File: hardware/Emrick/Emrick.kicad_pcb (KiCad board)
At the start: 4 copper layers, 41.5 x 74.1 mm, 88 parts, among them J1 LED_STRIP_CONNECTOR, J2 UFL, J3 Conn_02x05_Odd_Even, J4 BATT_CONN, P1 USB_C_Plug_USB2.0, Q1 Q_NMOS_GSD, Q2 Q_NMOS_GSD, Q3 Q_NMOS_GSD, SW1 SW_SPST, U1 74HCT541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

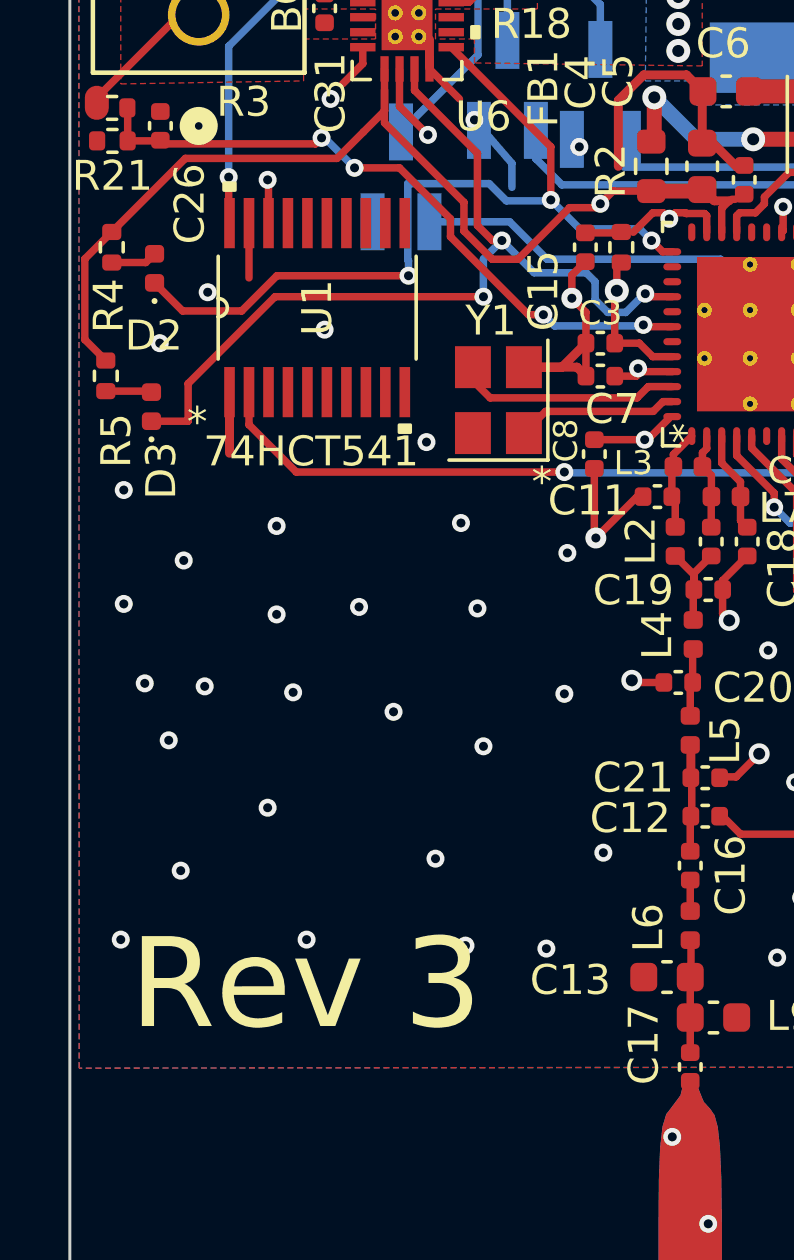
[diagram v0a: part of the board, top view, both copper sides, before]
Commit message: Fix floating GND connection
Added a via to fix a floating GND fill that wasn't connecting the GND pin of the battery voltage divider.
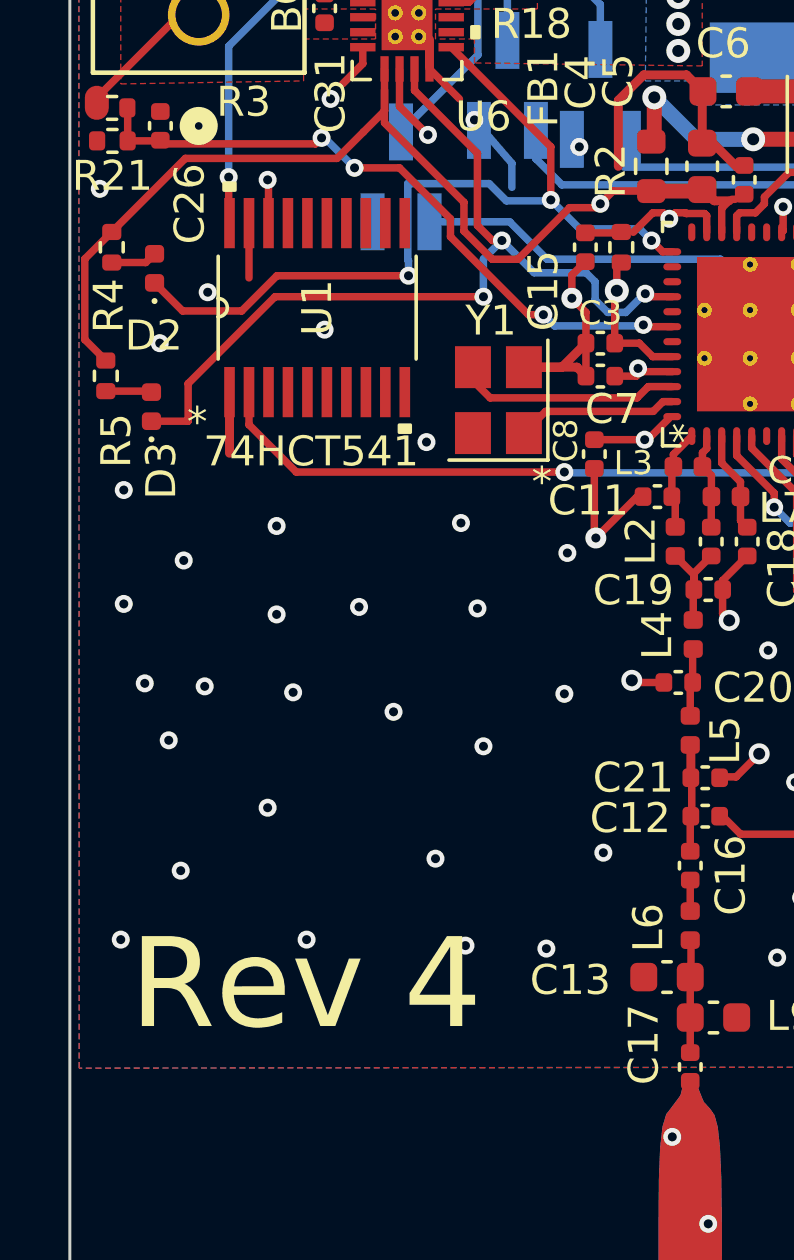
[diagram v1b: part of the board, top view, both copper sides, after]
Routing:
- net GND: vias 86 -> 87
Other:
- board text added: "Rev 4"
- board text removed: "Rev 3"
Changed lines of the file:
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@@
     (title "Emrick")
     (date "2022-10-13")
-    (rev "3")
+    (rev "4")
     (company "Erik Duxstad, Zareef Huq")
     (comment 1 "Layer Stackup: JLC04161H-7628")
@@
     (effects (font (size 1 1) (thickness 0.15)))
   )
-  (gr_text "Rev 3" (at 83.7 63.1) (layer "F.SilkS")
+  (gr_text "Rev 4" (at 83.7 63.1) (layer "F.SilkS")
     (effects (font (size 3 3) (thickness 0.3)) (justify left bottom))
   )
@@
   (via (at 109.95 34.7) (size 0.6) (drill 0.3) (layers "F.Cu" "B.Cu") (net 2))
   (via (at 91.35 48.75) (size 0.6) (drill 0.3) (layers "F.Cu" "B.Cu") (free) (net 2))
+  (via (at 82.7 34.8) (size 0.6) (drill 0.3) (layers "F.Cu" "B.Cu") (free) (net 2))
   (via (at 112.3 58.45) (size 0.6) (drill 0.3) (layers "F.Cu" "B.Cu") (free) (net 2))
   (via (at 111 44.05) (size 0.6) (drill 0.3) (layers "F.Cu" "B.Cu") (net 2))

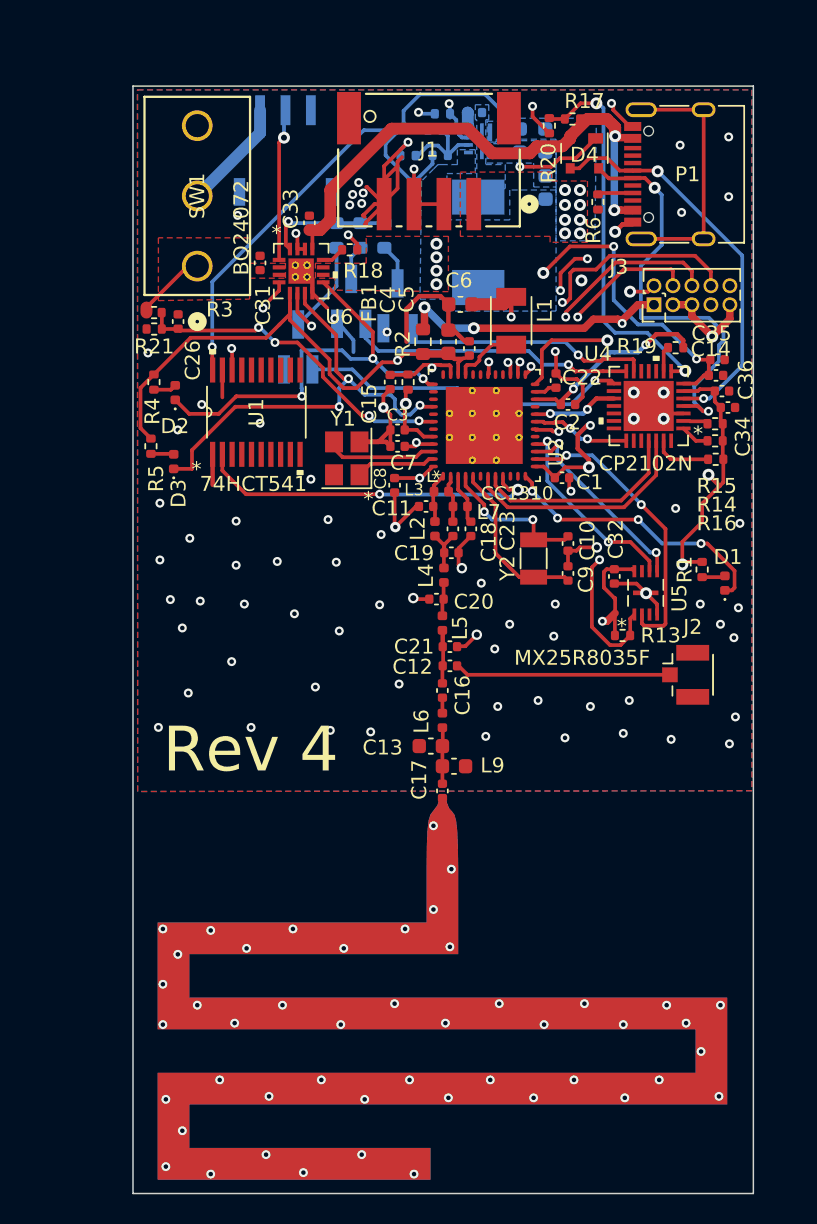
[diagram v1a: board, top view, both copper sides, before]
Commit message: Update schematic and pcb to revision 4
- Add a new switch footprint
- Add a line to reset the CC1310 from the CP2102x
- Switch to a 433MHz - 510MHz antenna
- Decrease the dimensions of the board
- Add a wireframe of the battery dimensions
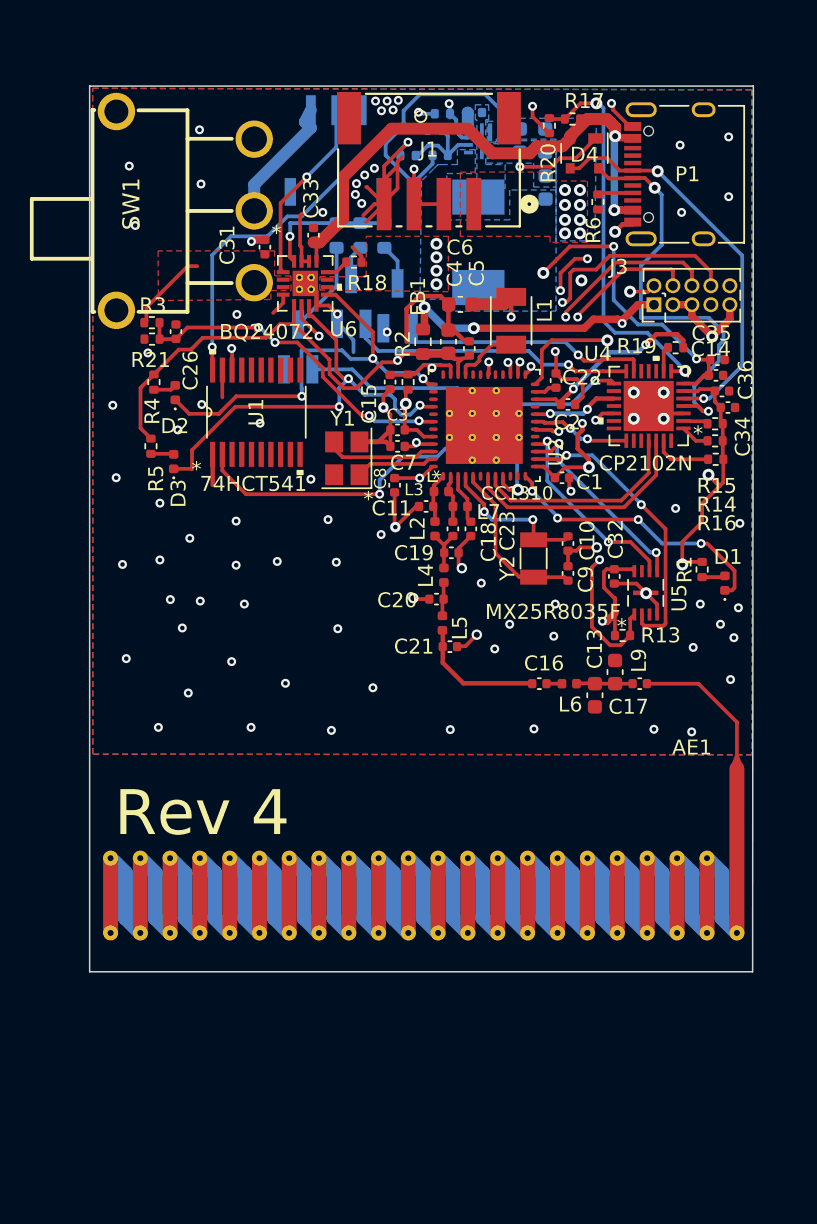
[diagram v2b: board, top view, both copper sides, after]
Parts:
- removed C12: ?, Capacitor_SMD:C_0402_1005Metric
- removed J2: UFL, Connector_Coaxial:U.FL_Hirose_U.FL-R-SMT-1_Vertical
- AE1: footprint Emrick Footprints:emrick_custom_antenna -> RF_Antenna:Texas_SWRA416_868MHz_915MHz
- C17: value 5.6pF -> 5.1pF
- SW1: footprint xkbswitch:SS-12D10G5_XKB -> xkbconnectivity:SW-TH_SS-12D11G4R
- moved C17 15.0 mm to (115.6, 56.9), turned to 0 degrees
- moved AE1 14.4 mm to (113.1, 67.8)
- moved L9 12.5 mm to (114.0, 56.1), turned to 90 degrees
- moved C13 11.5 mm to (112.6, 57.7), turned to -90 degrees
- moved L6 8.83 mm to (110.9, 56.9), turned to 0 degrees
- moved C16 6.50 mm to (108.9, 56.9), turned to 180 degrees
- moved SW1 3.78 mm to (85.2, 25.3)
- moved J4 3.40 mm to (95.3, 22.0)
- moved C31 1.10 mm to (90.5, 27.7)
- moved R18 0.87 mm to (96.5, 28.7)
- moved U6 0.87 mm to (93.2, 30.1)
- moved C33 0.87 mm to (93.8, 26.9)
- moved R21 0.69 mm to (83.0, 33.9)
- moved C26 0.69 mm to (84.6, 33.4)
- moved R3 0.69 mm to (83.0, 32.8)
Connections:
- U4 pad 19: unconnected-(U4-GPIO-0/TXT-Pad19) -> WMCU_RESET
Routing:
- net Net-(J2-Pin_1): track 14.4 -> 0.00 mm
- net GND: track 113.8 -> 99.7 mm, vias 87 -> 92
- net WMCU_RESET: track 29.7 -> 42.6 mm, vias 3 -> 4
- net Net-(AE1-A): track 0.00 -> 9.36 mm
- net Net-(C16-Pad2): track 3.32 -> 8.74 mm
- net LED_DATA_3V: track 23.5 -> 27.4 mm
- net VDDS: track 122.0 -> 119.5 mm
- net BAT_TS: track 10.2 -> 12.5 mm
- net VBAT: track 4.89 -> 6.25 mm
- net Net-(J4-Pin_3): track 7.47 -> 8.57 mm
- net 5V: track 42.6 -> 43.7 mm
- net LED_DATA_5V: track 26.0 -> 25.0 mm
- net BAT_PGOOD: track 30.1 -> 29.3 mm
- net BAT_CHG: track 28.9 -> 28.3 mm
- net HALF_VBAT: track 22.4 -> 23.0 mm
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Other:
- board size 41.5 x 74.1 mm -> 44.4 x 59.2 mm
- board text added: "41.5 by 52.0 mm"
- board text added: "Battery Dimensions"

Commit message: Finalize revision 4
- Added rev4 bom
- Updated production files in hardware\Emrick\production
- Fixed/ignored all errors in board PCB
- Added AAMB graphics
- Changed connector to JST PA 4 pin for mechanical latch
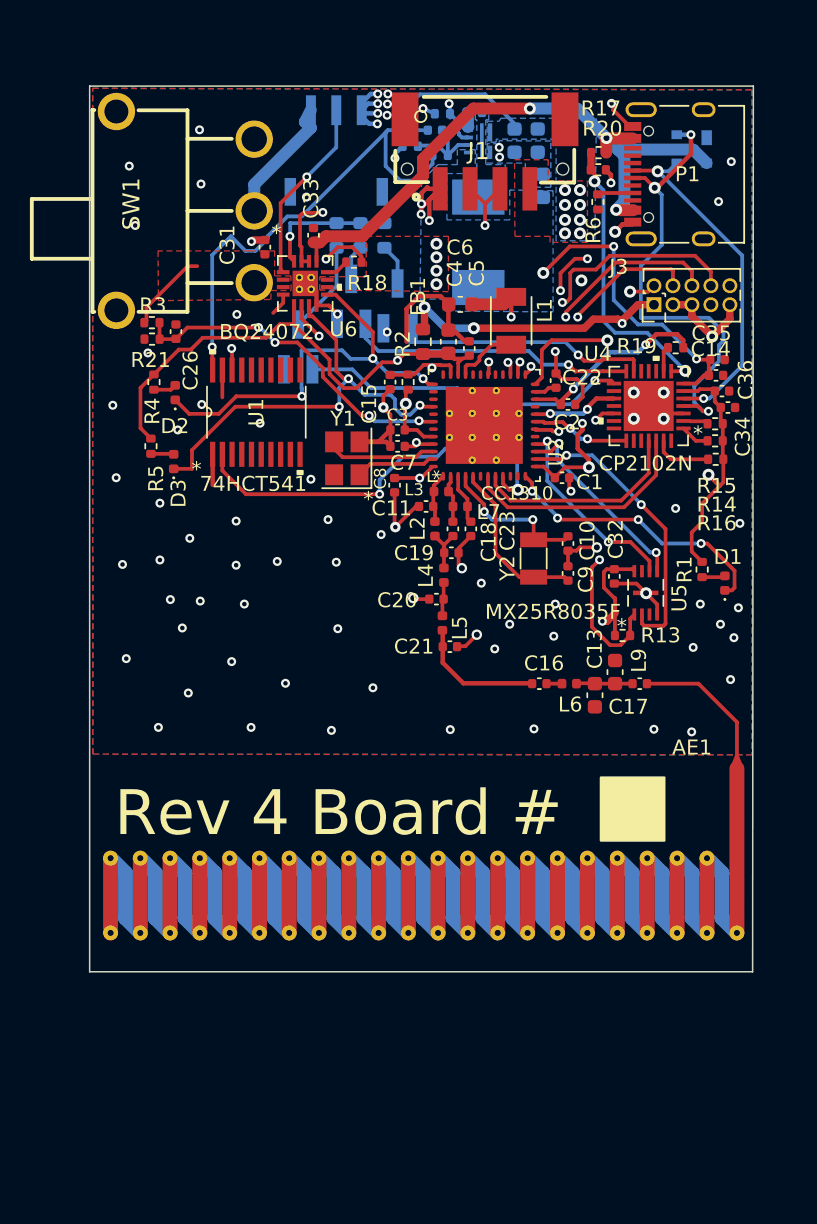
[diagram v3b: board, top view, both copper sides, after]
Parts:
- D4: moved to B.Cu
- J1: footprint s4bjstconn:CONN_S4B-PH-SM4-TBLFSN_JST -> jstpa:CONN-SMD_BM04B-PASS-1-TFT
- moved D4 7.18 mm to (119.1, 21.1), turned to 180 degrees
- moved R20 4.41 mm to (112.8, 22.6), turned to 0 degrees
- moved J1 3.77 mm to (105.2, 21.5), turned to 180 degrees
- moved R17 2.85 mm to (112.8, 21.4)
- moved R12 0.64 mm to (100.2, 21.0)
- moved C30 0.51 mm to (108.8, 20.6)
- moved C29 0.36 mm to (107.2, 20.6)
- moved C25 0.21 mm to (109.1, 23.6)
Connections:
- J1 pad 1: 5V -> GND
- J1 pad 4: GND -> 5V
- J1 pad 5: (no net) -> GND
- J1 pad 6: (no net) -> GND
- J4 pad 4: (no net) -> GND
- J4 pad 5: (no net) -> GND
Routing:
- net GND: track 99.7 -> 88.0 mm, vias 92 -> 93
- net Net-(U4-VBUS): track 26.3 -> 19.5 mm
- net VBUS: track 37.4 -> 41.9 mm, vias 2 -> 3
- net USB_DMINUS: track 26.7 -> 23.4 mm
- net USB_DPLUS: track 28.5 -> 31.2 mm, vias 2 -> 3
- net VDDS: track 119.5 -> 118.0 mm, vias 8 -> 7
- net LED_DATA_5V: track 25.0 -> 26.3 mm
- net 5V: track 43.7 -> 44.2 mm
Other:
- board text added: "Emrick Rev 4 7/29/2023"
- board text added: "Rev 4 Board #"
- board text removed: "Emrick Rev 3 5/4/2023 Sam Dlott Erik Duxstad Zareef Huq Hamza Kamel"
- board text removed: "Rev 4"

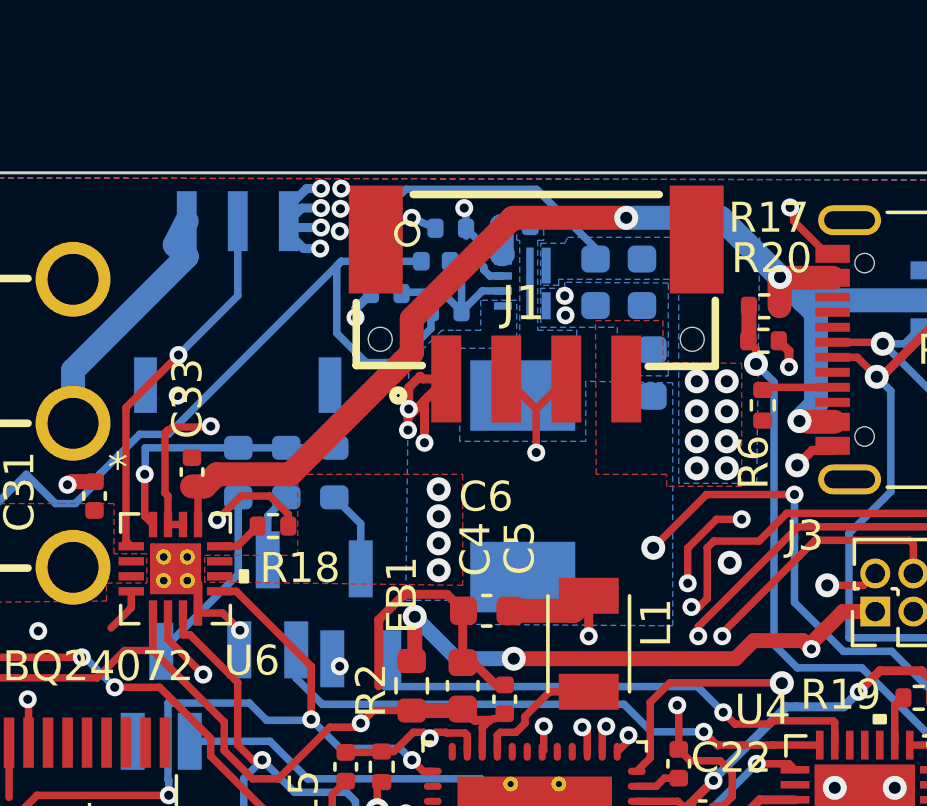
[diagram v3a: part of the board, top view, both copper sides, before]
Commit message: update bom and change to horizontal PA connector footprint
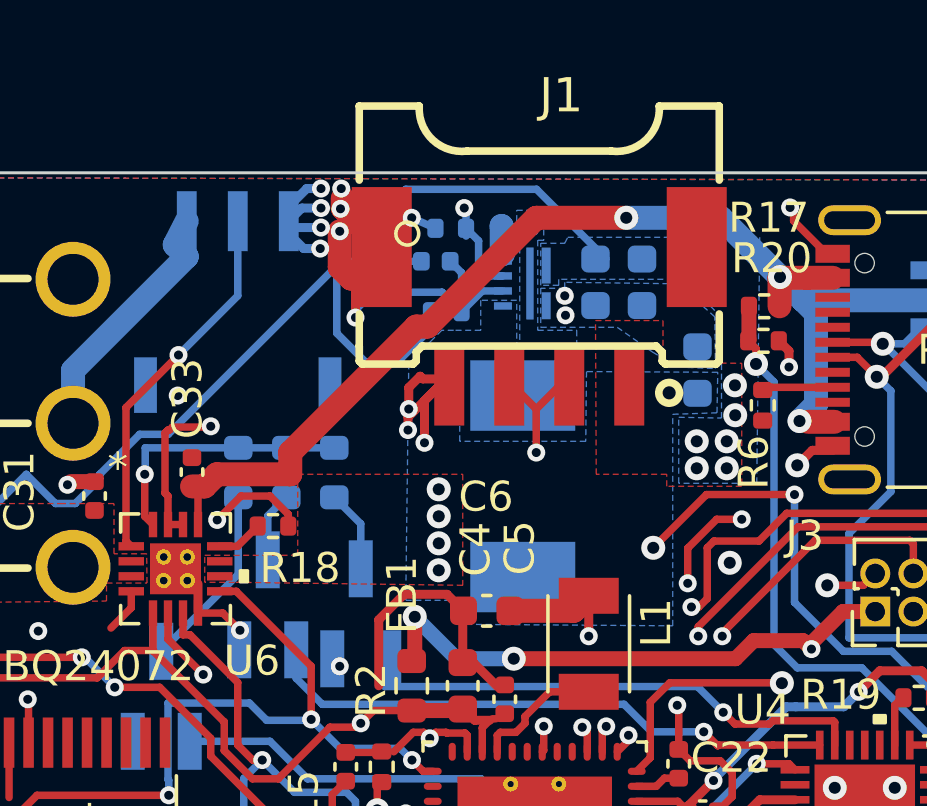
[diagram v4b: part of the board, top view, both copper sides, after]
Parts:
- J1: footprint jstpa:CONN-SMD_BM04B-PASS-1-TFT -> jstpa:CONN-SMD_SM04B-PASS-TBT-LF-SN
- moved C25 1.50 mm to (110.6, 23.5)
- moved J1 0.25 mm to (105.3, 21.7), turned to 0 degrees
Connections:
- J1 pad 1: GND -> 5V
- J1 pad 4: 5V -> GND
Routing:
- net GND: track 88.0 -> 96.1 mm
- net 5V: vias 9 -> 7
